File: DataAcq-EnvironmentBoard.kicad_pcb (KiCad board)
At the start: 2 copper layers, 56.1 x 59 mm, 37 parts, among them J1 Airflow Breakout, J2 CAN Output, J3 CAN Input, J4 Humidity Breakout, J5 Temp Breakout, U1 SHT45, U2 FS3000-1005, U3 LMT87DCK, U4 Daughterboard Connector

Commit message: rm useless stuff
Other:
- board text removed: "2_SCL"
- board text removed: "2_SDA"
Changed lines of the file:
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@@
 		(fp_arc
 			(start 18.037742 -21.812258)
-			(mid 20.300485 -20.874999)
+			(mid 20.300482 -20.874999)
 			(end 21.237742 -18.612258)
 			(stroke
@@
 		)
 	)
-	(gr_text "2_SDA"
-		(at 140.8 85.4 270)
-		(layer "F.SilkS" knockout)
-		(effects
-			(font
-				(size 1 1)
-				(thickness 0.153)
-			)
-			(justify left bottom)
-		)
-	)
 	(gr_text "Humidity Breakout"
 		(at 194.25 117.5 90)
@@
 		(layer "F.SilkS" knockout)
 		(effects
-			(font
-				(size 1 1)
-				(thickness 0.153)
-			)
-			(justify left bottom)
-		)
-	)
-	(gr_text "2_SCL"
-		(at 140.8 98.2 270)
-		(layer "F.SilkS" knockout)
-		(effects

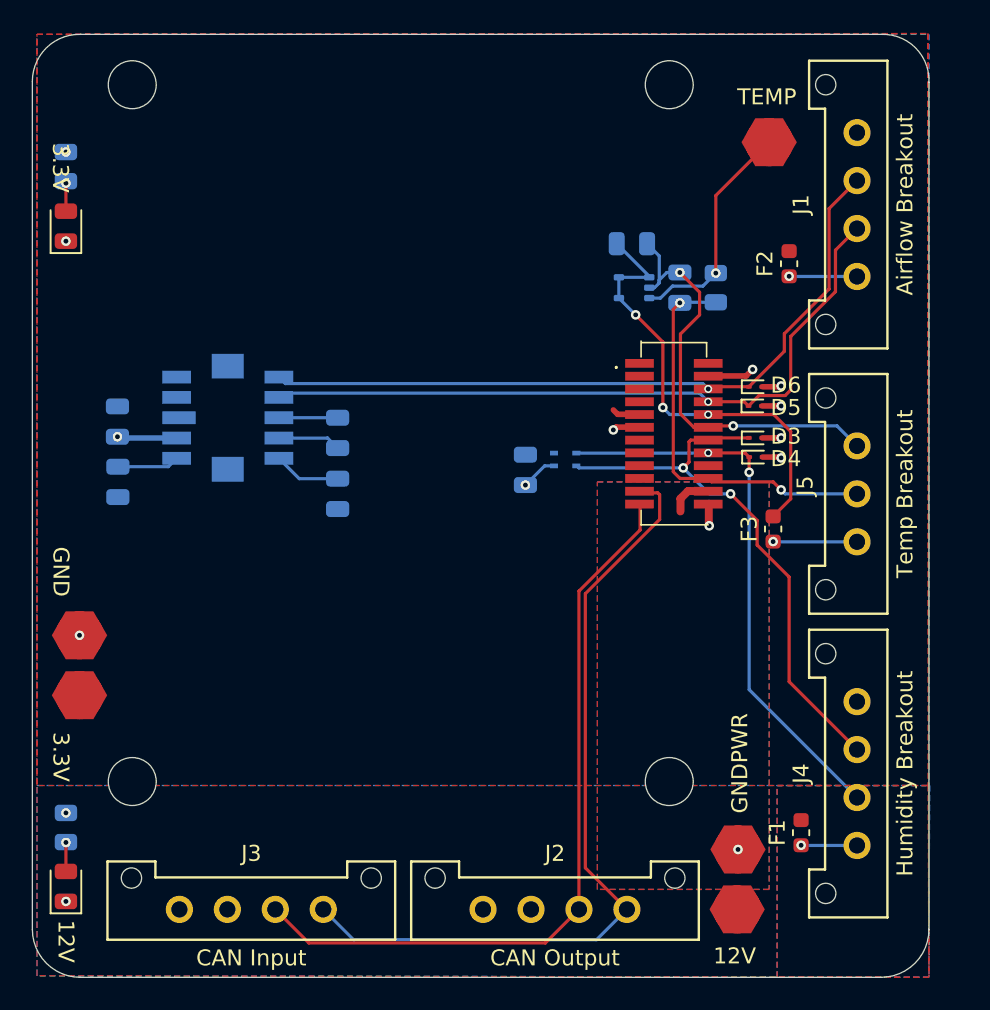
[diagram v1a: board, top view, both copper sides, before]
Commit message: start sch/layout modifications
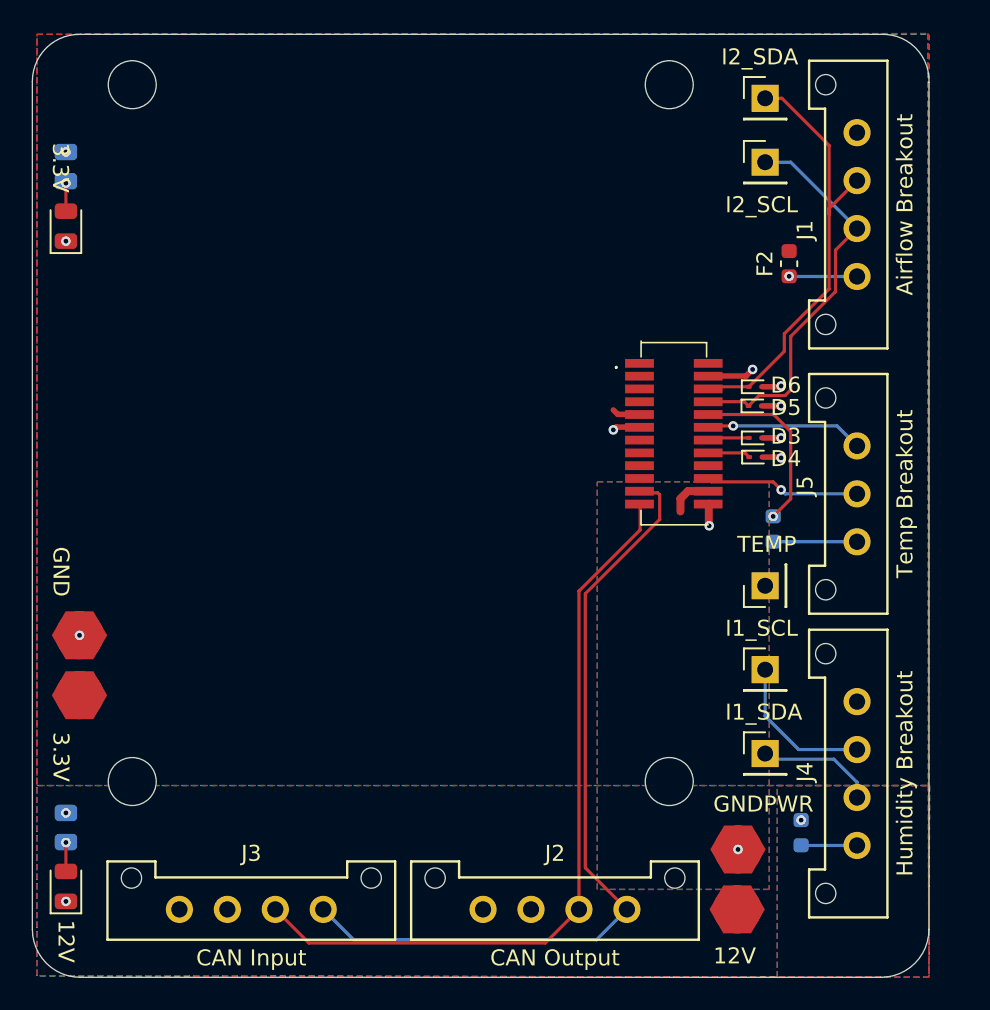
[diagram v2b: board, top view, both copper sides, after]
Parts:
- removed C1, C2, C3, C5, C7: 0.1uF, Capacitor_SMD:C_0805_2012Metric
- removed C4, C6: 1uF, Capacitor_SMD:C_0805_2012Metric
- removed R1: 1k, Resistor_SMD:R_0805_2012Metric
- removed U1: SHT45, Sensor_Humidity:Sensirion_DFN-4_1.5x1.5mm_P0.8mm_SHT4x_NoCentralPad
- removed U2: FS3000-1005, SamacSys_Parts:FS30001005
- removed U3: LMT87DCK, Package_TO_SOT_SMD:SOT-353_SC-70-5
- added TP6: TestPoint, Connector_PinHeader_2.54mm:PinHeader_1x01_P2.54mm_Vertical, F.Cu at (185.5, 116.2)
- added TP7: TestPoint, Connector_PinHeader_2.54mm:PinHeader_1x01_P2.54mm_Vertical, F.Cu at (185.5, 111.0)
- added TP8: TestPoint, Connector_PinHeader_2.54mm:PinHeader_1x01_P2.54mm_Vertical, F.Cu at (185.5, 75.2)
- added TP9: TestPoint, Connector_PinHeader_2.54mm:PinHeader_1x01_P2.54mm_Vertical, F.Cu at (185.5, 79.2)
- F1, F3: moved to B.Cu
- TP3: footprint UTSVT_Special:TestPoint_HEX_3mmID -> Connector_PinHeader_2.54mm:PinHeader_1x01_P2.54mm_Vertical
- moved TP3 27.8 mm to (185.5, 105.8)
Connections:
- TP3 pad 1: /TEMP_OUT -> /PA1(ADC)
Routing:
- net /I2C1_SDA: track 35.0 -> 10.1 mm, vias 2 -> 0
- net /I2C1_SCL: track 35.3 -> 12.1 mm, vias 2 -> 0
- net /I2C2_SCL: track 44.7 -> 25.0 mm, vias 1 -> 0
- net /I2C2_SDA: track 45.5 -> 27.8 mm, vias 1 -> 0
- net VDDA: track 28.5 -> 11.4 mm, vias 3 -> 1
- net GNDA: track 26.9 -> 9.87 mm, vias 2 -> 1
- net /PA1(ADC): track 25.1 -> 9.71 mm, vias 2 -> 1
- net /TEMP_OUT: track 14.4 -> 0.00 mm, vias 1 -> 0
- net +3.3V: track 7.81 -> 1.79 mm, vias 3 -> 2
- net /AFLW_VCM: track 4.20 -> 0.00 mm
- net /AFLW_TP2: track 3.94 -> 0.00 mm
- net /AFLW_VREG: track 3.89 -> 0.00 mm
- net /AFLW_TP1: track 3.68 -> 0.00 mm
- net Net-(J5-Pin_1): vias 1 -> 0
- net Net-(J4-Pin_1): vias 1 -> 0
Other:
- board text added: "I1_SCL"
- board text added: "I1_SDA"
- board text added: "I2_SCL"
- board text added: "I2_SDA"

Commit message: update BOM and model
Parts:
- removed LOGO1: Arrow, images:arrow
- moved LOGO3 8.49 mm to (160.8, 93.5)
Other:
- board text removed: "Airflow"
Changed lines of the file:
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@@
 		(fp_arc
 			(start 18.037742 -21.812258)
-			(mid 20.300485 -20.874999)
+			(mid 20.300482 -20.874999)
 			(end 21.237742 -18.612258)
 			(stroke
@@
 	(footprint "UTSVT_Special:UTSVT_Logo_Symbol"
 		(layer "B.Cu")
-		(at 162.75 85.25 180)
+		(at 160.75 93.5 180)
 		(property "Reference" "LOGO3"
 			(at 0 0 0)
@@
 		)
 	)
-	(footprint "images:arrow"
-		(layer "B.Cu")
-		(at 151.93774 86.5 180)
-		(property "Reference" "LOGO1"
-			(at 0 0 0)
-			(layer "B.SilkS")
-			(hide yes)
-			(effects
-				(font
-					(size 1.5 1.5)
-					(thickness 0.3)
-				)
-				(justify mirror)
-			)
-		)
-		(property "Value" "Arrow"
-			(at 0.75 0 0)
-			(layer "B.SilkS")
-			(hide yes)
-			(effects
-				(font
-					(size 1.5 1.5)
-					(thickness 0.3)
-				)
-				(justify mirror)
-			)
-		)
-		(property "Footprint" "images:arrow"
-			(at 0 0 0)
-			(layer "B.Fab")
-			(effects
-				(font
-					(size 1.27 1.27)
-					(thickness 0.15)
-				)
-				(justify mirror)
-			)
-		)
-		(property "Datasheet" ""
-			(at 0 0 0)
-			(layer "B.Fab")
-			(hide yes)
-			(effects
-				(font
-					(size 1.27 1.27)
-					(thickness 0.15)
-				)
-				(justify mirror)
-			)
-		)
-		(property "Description" "Graph footprint placeholder"
-			(at 0 0 0)
-			(layer "B.Fab")
-			(hide yes)
-			(effects
-				(font
-					(size 1.27 1.27)
-					(thickness 0.15)
-				)
-				(justify mirror)
-			)
-		)
-		(sheetname "Root")
-		(sheetfile "DataAcq-EnvironmentBoard.kicad_sch")
-		(attr board_only exclude_from_pos_files)
-		(fp_poly
-			(pts
-				(xy 0.726813 2.535378) (xy 0.729184 2.530342) (xy 0.731327 2.521638) (xy 0.733254 2.508219) (xy 0.734975 2.489032)
-				(xy 0.736503 2.46303) (xy 0.737848 2.429161) (xy 0.739021 2.386377) (xy 0.740035 2.333627) (xy 0.740899 2.269861)
-				(xy 0.741626 2.19403) (xy 0.742226 2.105083) (xy 0.742712 2.001972) (xy 0.743094 1.883645) (xy 0.743383 1.749054)
-				(xy 0.743591 1.597149) (xy 0.743729 1.426879) (xy 0.743808 1.237195) (xy 0.74384 1.027047) (xy 0.743842 0.949245)
-				(xy 0.743842 -0.612576) (xy 1.307192 -0.612576) (xy 1.432646 -0.612599) (xy 1.538052 -0.612713)
-				(xy 1.625238 -0.612988) (xy 1.696035 -0.613491) (xy 1.752272 -0.614291) (xy 1.795778 -0.615455)
-				(xy 1.828382 -0.617054) (xy 1.851914 -0.619154) (xy 1.868203 -0.621825) (xy 1.879079 -0.625134)
-				(xy 1.88637 -0.629151) (xy 1.891907 -0.633943) (xy 1.89242 -0.634453) (xy 1.908726 -0.657149) (xy 1.914298 -0.675403)
-				(xy 1.906693 -0.685945) (xy 1.884645 -0.710682) (xy 1.849305 -0.748466) (xy 1.801823 -0.798148)
-				(xy 1.74335 -0.858578) (xy 1.675038 -0.928607) (xy 1.598036 -1.007087) (xy 1.513495 -1.092867) (xy 1.422566 -1.1848)
-				(xy 1.3264 -1.281735) (xy 1.226148 -1.382523) (xy 1.122959 -1.486016) (xy 1.017986 -1.591063) (xy 0.912378 -1.696517)
-				(xy 0.807287 -1.801228) (xy 0.703862 -1.904046) (xy 0.603256 -2.003823) (xy 0.506618 -2.09941) (xy 0.415099 -2.189656)
-				(xy 0.32985 -2.273414) (xy 0.252021 -2.349533) (xy 0.182764 -2.416865) (xy 0.12323 -2.474261) (xy 0.074567 -2.520571)
-				(xy 0.037929 -2.554647) (xy 0.014464 -2.575338) (xy 0.005547 -2.581568) (xy -0.005854 -2.573785)
-				(xy -0.03239 -2.550553) (xy -0.073883 -2.512047) (xy -0.130153 -2.458442) (xy -0.201022 -2.389912)
-				(xy -0.28631 -2.306633) (xy -0.385838 -2.208779) (xy -0.499429 -2.096526) (xy -0.626901 -1.970047)
-				(xy -0.768078 -1.829519) (xy -0.922779 -1.675116) (xy -0.959735 -1.638178) (xy -1.118104 -1.479694)
-				(xy -1.261108 -1.336259) (xy -1.389006 -1.207606) (xy -1.502058 -1.093472) (xy -1.600521 -0.99359)
-				(xy -1.684656 -0.907695) (xy -1.75472 -0.835522) (xy -1.810975 -0.776805) (xy -1.853678 -0.73128)
-				(xy -1.883088 -0.69868) (xy -1.899466 -0.678741) (xy -1.903359 -0.671786) (xy -1.895571 -0.646555)
-				(xy -1.883355 -0.630679) (xy -1.87727 -0.626625) (xy -1.867536 -0.623219) (xy -1.852359 -0.620406)
-				(xy -1.829945 -0.61813) (xy -1.798498 -0.616336) (xy -1.756225 -0.614968) (xy -1.701331 -0.61397)
-				(xy -1.632023 -0.613288) (xy -1.546505 -0.612865) (xy -1.442983 -0.612647) (xy -1.319663 -0.612577)
-				(xy -1.298126 -0.612576) (xy -0.732903 -0.612576) (xy -0.732903 0.958678) (xy -0.732892 1.175454)
-				(xy -0.732852 1.371411) (xy -0.73277 1.547607) (xy -0.732632 1.705101) (xy -0.732427 1.844952) (xy -0.732141 1.968217)
-				(xy -0.731762 2.075956) (xy -0.731276 2.169227) (xy -0.730672 2.249089) (xy -0.729936 2.3166) (xy -0.729055 2.372819)
-				(xy -0.728017 2.418803) (xy -0.726809 2.455613) (xy -0.725418 2.484306) (xy -0.723831 2.50594) (xy -0.722036 2.521575)
-				(xy -0.72002 2.532269) (xy -0.717769 2.53908) (xy -0.715272 2.543067) (xy -0.71376 2.544462) (xy -0.706067 2.54749)
-				(xy -0.690596 2.550094) (xy -0.66591 2.552305) (xy -0.630575 2.55415) (xy -0.583155 2.555661) (xy -0.522216 2.556867)
-				(xy -0.446322 2.557797) (xy -0.354039 2.558481) (xy -0.243932 2.558949) (xy -0.114565 2.55923) (xy 0.007584 2.559342)
-				(xy 0.709785 2.55969)
-			)
-			(stroke
-				(width 0)
-				(type solid)
-			)
-			(fill solid)
-			(layer "B.SilkS")
-		)
-	)
 	(footprint "Resistor_SMD:R_0805_2012Metric"
 		(layer "B.Cu")
@@
 		)
 	)
-	(gr_text "Airflow"
-		(at 151.93227 83 0)
-		(layer "B.SilkS")
-		(effects
-			(font
-				(size 1 1)
-				(thickness 0.153)
-			)
-			(justify mirror)
-		)
-	)

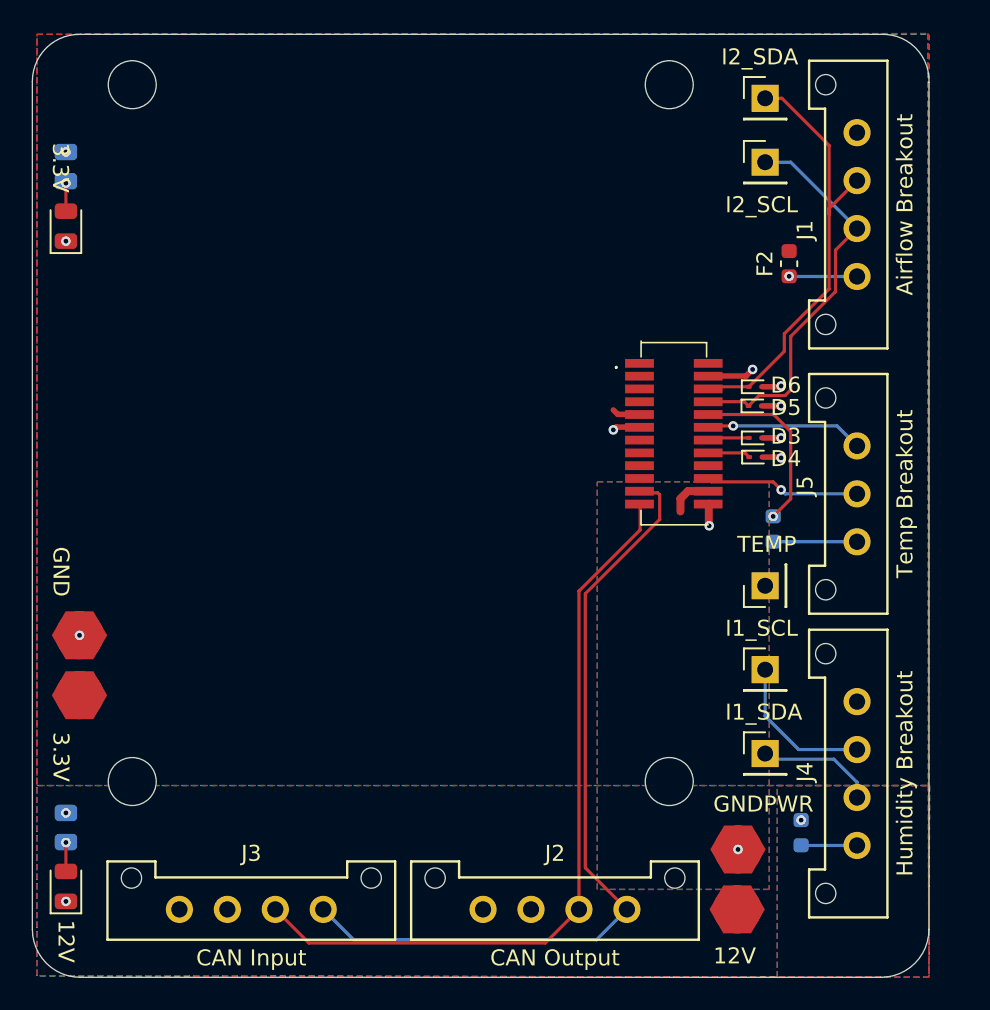
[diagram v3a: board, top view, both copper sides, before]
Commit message: fix trace routing
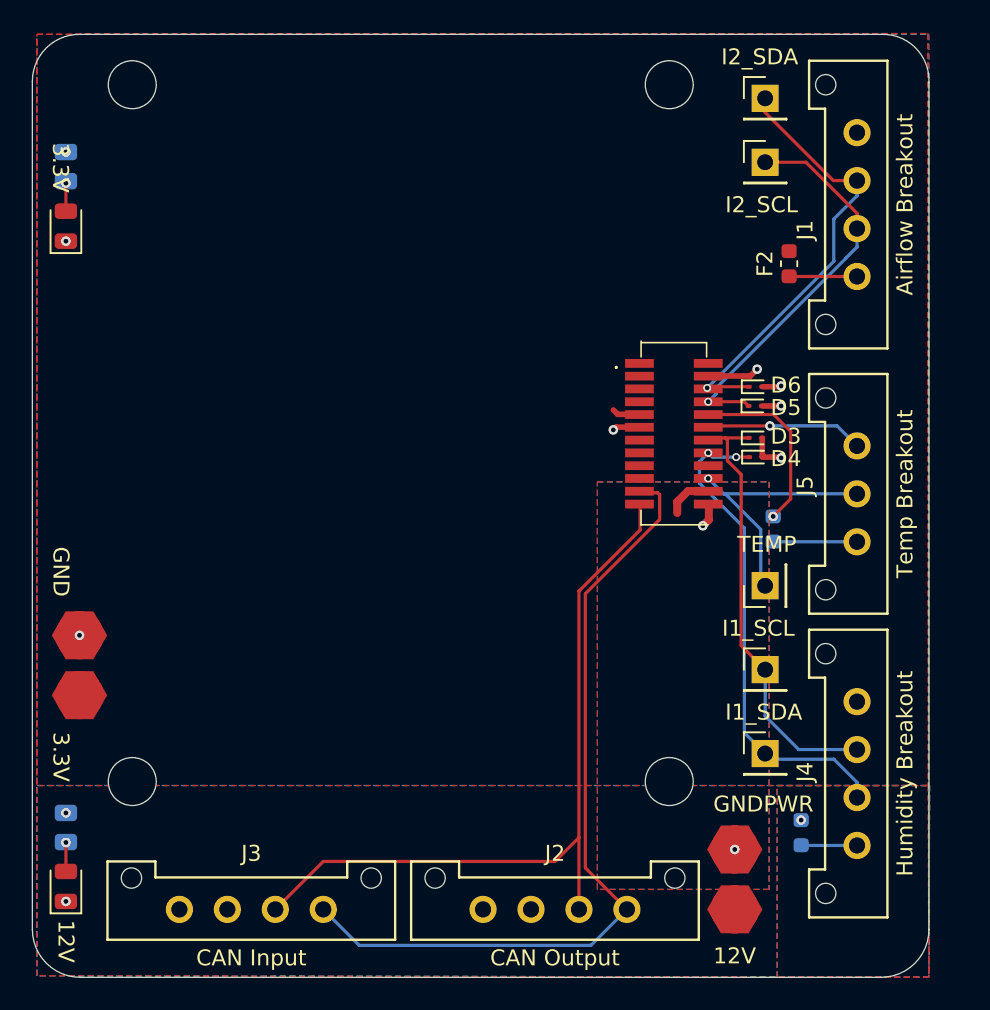
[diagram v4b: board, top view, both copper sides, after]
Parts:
- moved TP2 0.20 mm to (183.6, 122.2)
- moved TP1 0.15 mm to (183.6, 126.0)
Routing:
- net /I2C1_SDA: track 10.1 -> 30.9 mm, vias 0 -> 2
- net /I2C1_SCL: track 12.1 -> 27.7 mm
- net /PA1(ADC): track 9.71 -> 16.6 mm
- net /I2C2_SCL: track 25.0 -> 25.4 mm, vias 0 -> 1
- net GND: track 9.42 -> 9.74 mm, vias 8 -> 7
- net /I2C2_SDA: track 27.8 -> 27.9 mm, vias 0 -> 1
- net Net-(J1-Pin_1): vias 1 -> 0

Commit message: silkscreen info
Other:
- board text added: "PSOM Connection"
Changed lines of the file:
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@@
+		)
+	)
+	(gr_text "PSOM Connection"
+		(at 175 96.2 90)
+		(layer "F.SilkS")
+		(effects
+			(font
+				(size 1 1)
+				(thickness 0.153)
+			)
 		)
 	)

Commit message: modify layout for new connector
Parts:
- removed F3: 250mA, Fuse:Fuse_0603_1608Metric
- removed J1: Airflow Breakout, UTSVT_Connectors:Molex_MicroFit3.0_1x4xP3.00mm_PolarizingPeg_Vertical
- removed J4: Humidity Breakout, UTSVT_Connectors:Molex_MicroFit3.0_1x4xP3.00mm_PolarizingPeg_Vertical
- removed J5: Temp Breakout, UTSVT_Connectors:Molex_MicroFit3.0_1x3xP3.00mm_PolarizingPeg_Vertical
- added J6: Breakout Connector, Connector_Molex:Molex_Nano-Fit_105310-xx10_2x05_P2.50mm_Vertical, F.Cu at (192.8, 101.7)
- F2: moved to B.Cu
- R2: moved to F.Cu
- moved TP4 57.5 mm to (185.2, 74.0)
- moved TP5 52.8 mm to (185.2, 77.8)
- moved D2 52.0 mm to (193.0, 74.8), turned to 180 degrees
- moved D1 51.4 mm to (193.1, 121.5), turned to 180 degrees
- moved R2 51.4 mm to (193.1, 123.5), turned to 180 degrees
- moved R3 51.3 mm to (193.0, 77.0), turned to 180 degrees
- moved TP3 27.1 mm to (191.8, 79.4)
- moved F1 17.3 mm to (192.0, 104.4), turned to 0 degrees
- moved F2 9.26 mm to (183.7, 94.2)
- moved TP6 8.81 mm to (185.2, 107.5)
- moved TP8 7.95 mm to (185.4, 83.2)
- moved TP9 7.48 mm to (191.8, 83.2)
- moved TP1 4.96 mm to (188.5, 125.2), turned to 90 degrees
- moved TP2 2.11 mm to (185.4, 123.4)
- moved TP7 1.68 mm to (185.4, 112.7)
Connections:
- F1 pad 2: Net-(J4-Pin_1) -> /3.3-out
- F2 pad 1: +3.3V -> /VDDA-out
- F2 pad 2: Net-(J1-Pin_1) -> VDDA
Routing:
- net /PA1(ADC): track 16.6 -> 43.1 mm
- net +3.3V: track 1.79 -> 20.2 mm
- net VDDA: track 11.4 -> 1.76 mm
- net /I2C1_SDA: track 30.9 -> 21.7 mm, vias 2 -> 0
- net /VDDA-out: track 0.00 -> 8.11 mm, vias 0 -> 1
- net /I2C2_SDA: track 27.9 -> 20.9 mm, vias 1 -> 0
- net GNDA: track 9.87 -> 16.7 mm, vias 1 -> 3
- net Net-(J5-Pin_1): track 5.26 -> 0.00 mm
- net Net-(J1-Pin_1): track 4.26 -> 0.00 mm
- net Net-(J4-Pin_1): track 3.51 -> 0.00 mm
- net /I2C1_SCL: track 27.7 -> 31.0 mm, vias 0 -> 1
- net /3.3-out: track 0.00 -> 2.71 mm
- net /I2C2_SCL: track 25.4 -> 22.9 mm
- net GND: track 9.74 -> 8.60 mm, vias 7 -> 6
- net Net-(D2-A): track 1.75 -> 2.26 mm
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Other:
- board size 56.1 x 59 mm -> 53 x 59 mm
- board text added: "Breakout"
- board text removed: "Airflow Breakout"
- board text removed: "Humidity Breakout"
- board text removed: "Temp Breakout"
